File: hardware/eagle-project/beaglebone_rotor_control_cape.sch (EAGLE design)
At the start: 29 parts, among them IC1 TLC2264CDU, IC2 MCP4901, IC3 MAX3232ESE, Q1 SQ2348ES-T1-GE3, Q2 SQ2348ES-T1-GE3, X1 BEAGLEBONE_OUTLINE

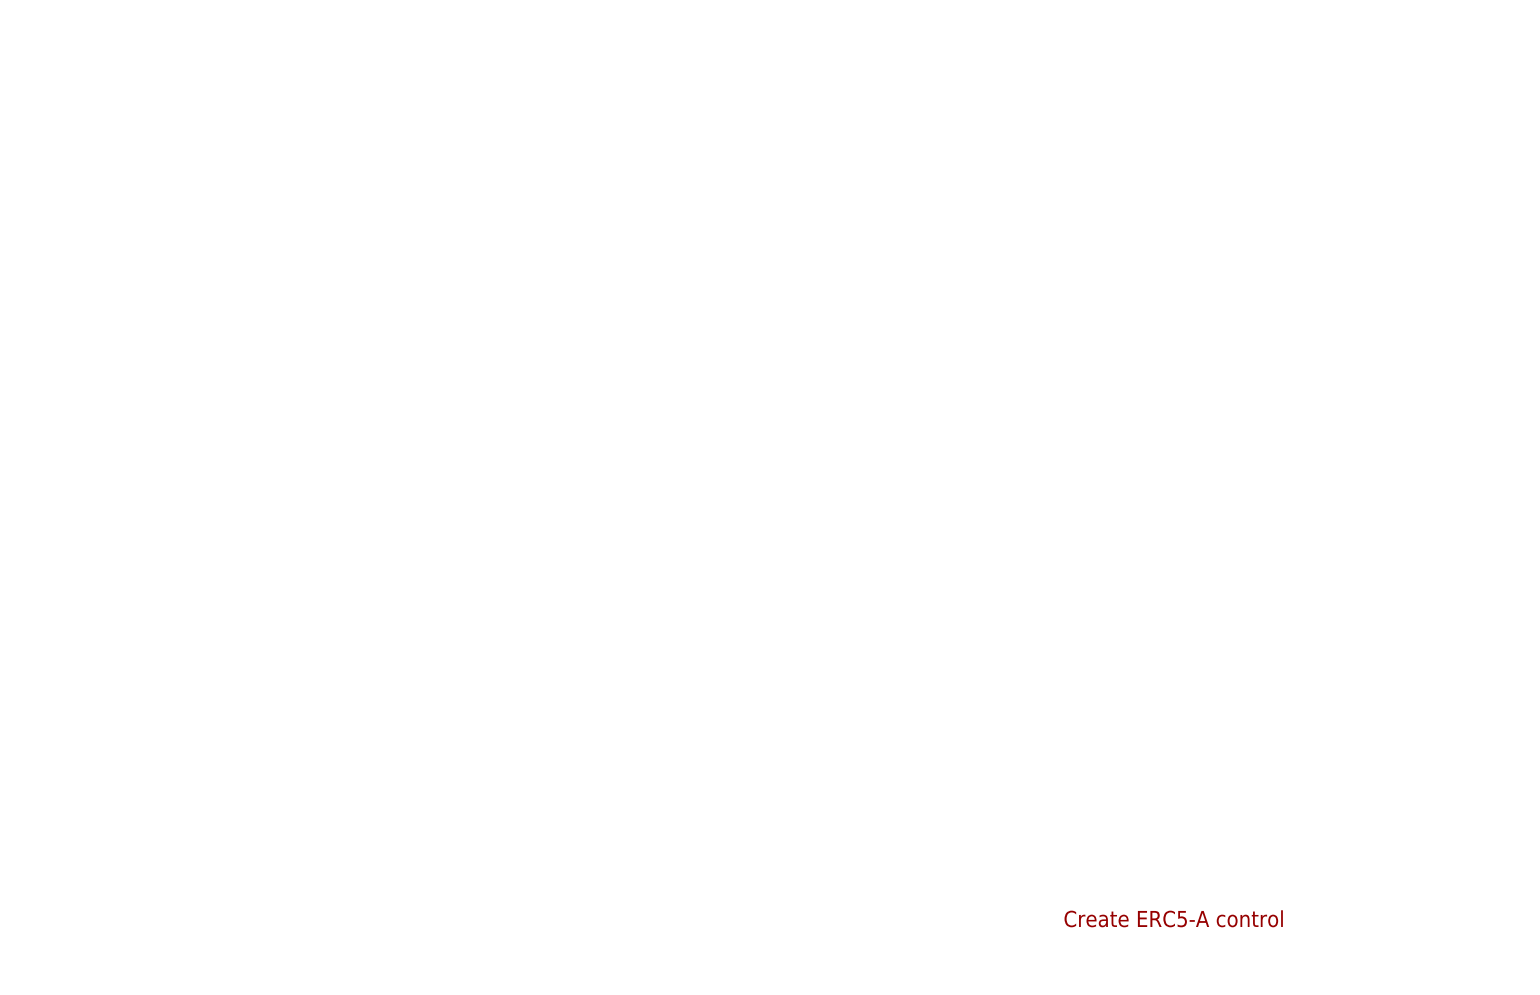
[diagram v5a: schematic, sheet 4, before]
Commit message: Hardware: Create ERC5-AP interface
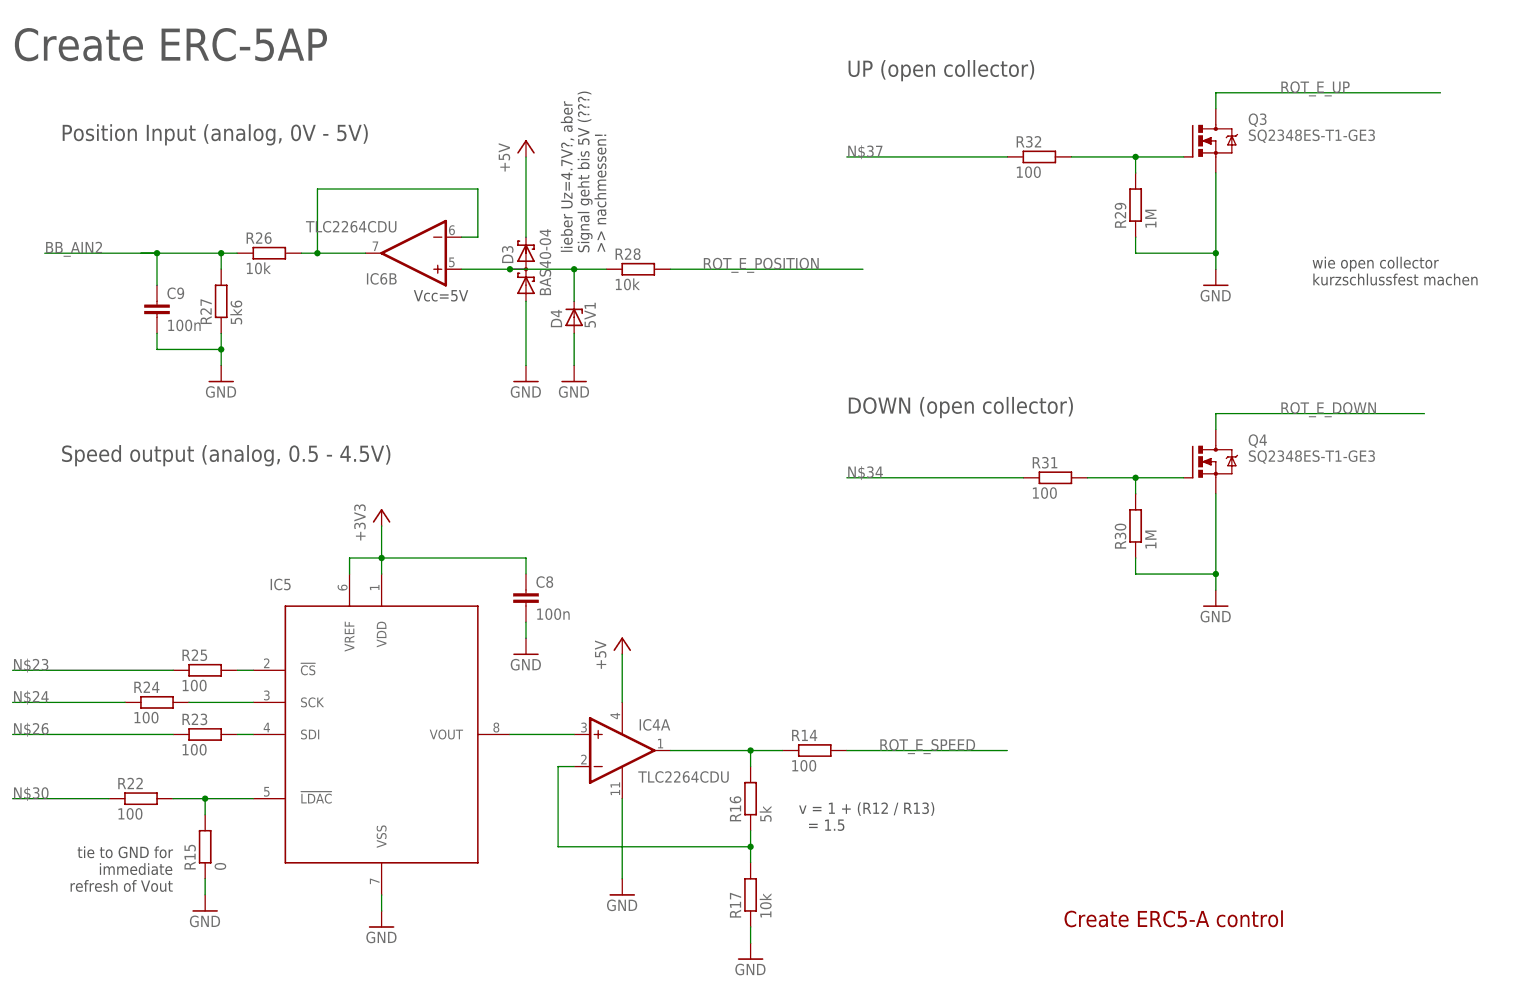
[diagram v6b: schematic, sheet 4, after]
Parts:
- added C8, C9: 100n, rcl:C-EUC0603
- added D3: BAS40-04, diode:BAS40-04
- added D4: 5V1, diode:ZENER-DIODESOT23
- added IC4, IC6: TLC2264CDU, ti-tlc2264cd:TLC2264CDU
- added IC5: MCP4901, microchip_mcp4901:MCP4901
- added Q3, Q4: SQ2348ES-T1-GE3, vishay_sq2348eS-t1-ge3:SQ2348ES-T1-GE3
- added R14, R18, R19, R20, R21, R22, R23, R24, R25, R31, R32: 100, rcl:R-EU_R0805
- added R15: 0, rcl:R-EU_R0805
- added R16: 5k, rcl:R-EU_R0805
- added R17, R26, R28: 10k, rcl:R-EU_R0805
- added R27: 5k6, rcl:R-EU_R0805
- added R29, R30: 1M, rcl:R-EU_R0805
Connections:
- new net BB_AIN2: C9.1, R26.1, R27.2
- new net N$10: IC2.SCK, R19.2
- new net N$23: R25.1
- new net N$24: R24.1
- new net N$26: R23.1
- new net N$27: IC5.SDI, R23.2
- new net N$28: IC5.SCK, R24.2
- new net N$29: IC5.!CS, R25.2
- new net N$30: R22.1
- new net N$31: IC4A.+IN, IC5.VOUT
- new net N$32: IC4A.OUT, R14.1, R16.2
- new net N$33: IC4A.-IN, R16.1, R17.2
- new net N$34: R31.1
- new net N$35: IC6B.-IN, IC6B.OUT, R26.2
- new net N$36: D3.C1A2, D4.C, IC6B.+IN, R28.1
- new net N$37: R32.1
- new net N$38: Q3.G, R29.2, R32.2
- new net N$39: Q4.G, R30.2, R31.2
- new net N$4: IC5.!LDAC, R15.2, R22.2
- new net N$6: IC2.!CS, R18.2
- new net N$8: R21.1
- new net N$9: IC2.SDI, R20.2
- new net ROT_E_DOWN: Q4.D
- new net ROT_E_POSITION: R28.2
- new net ROT_E_SPEED: R14.2
- new net ROT_E_UP: Q3.D
- net +3V3: now also C7.1, C8.1, IC2.VDD, IC2.VREF, IC5.VDD, IC5.VREF
- net +5V: now also D3.C2, IC4P.V+; no longer C7.1, IC2.VDD, IC2.VREF
- net BB_SPI0_CS0: now also R18.1; no longer IC2.!CS
- net BB_SPI0_D0: now also R20.1; no longer IC2.SDI
- net BB_SPI0_SCLK: now also R19.1; no longer IC2.SCK
- net GND: now also C8.2, C9.2, D3.A1, D4.A, IC4P.V-, IC5.VSS, Q3.S, Q4.S, R15.1, R17.1, R27.1, R29.1, R30.1
- net N$7: now also R21.2
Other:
- note added: "Create ERC-5AP"
- note added: "DOWN (open collector)"
- note added: "UP (open collector)"
- note removed: "no need for high accurancy, maybe read this voltage for reference with ADC?"
- note removed: "todo: Verstärker von 3.3V auf 5V range"
- moved on the sheet: C7, IC1A, IC2, R11, R12, R13, R9
